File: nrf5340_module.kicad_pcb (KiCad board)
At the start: 4 copper layers, 18.5 x 33 mm, 54 parts, among them J1 U.FL_A-1JB, J2 Conn_01x15, J3 Conn_01x15, J4 Conn_ARM_JTAG_SWD_10, Q1 Q_PMOS_GSD, U1 nrf5340, U2 AP2112K-3.3, Y1 32.768kHz, Y2 32MHz

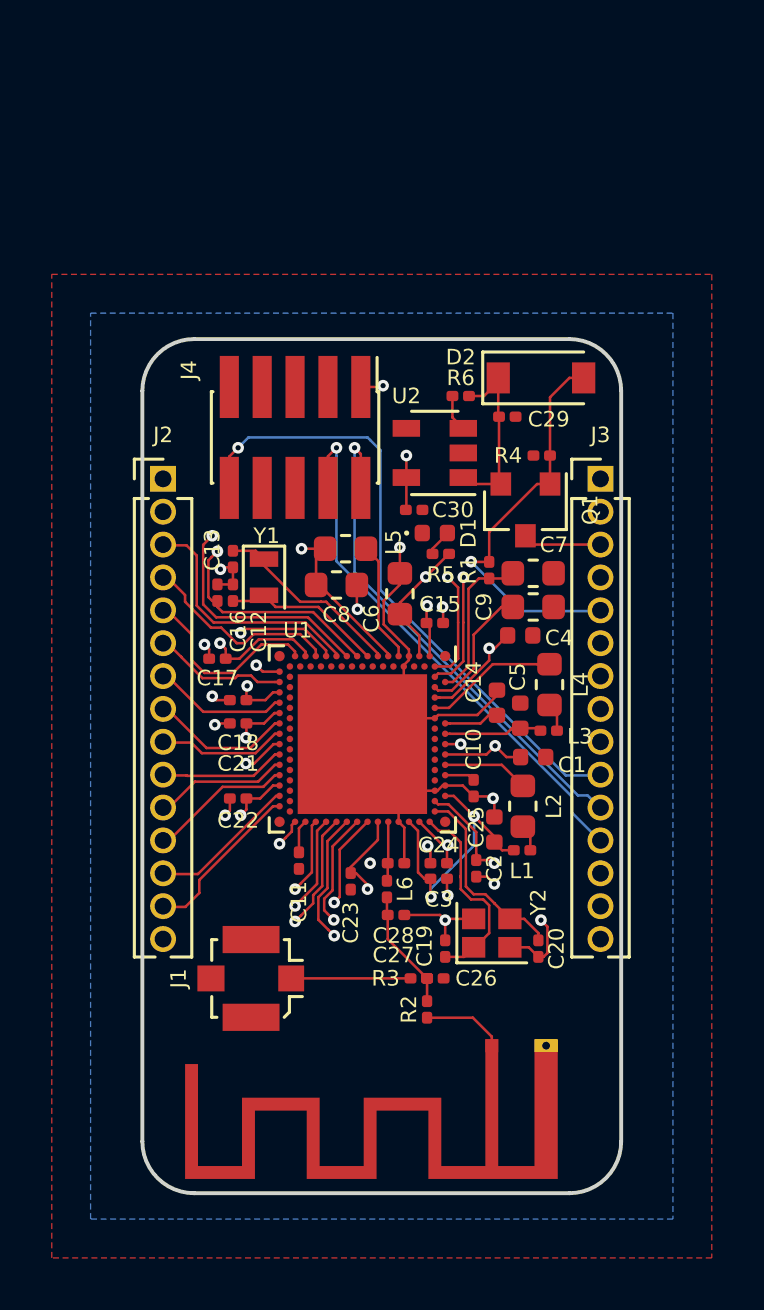
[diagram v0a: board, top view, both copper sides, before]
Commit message: added keepout, stitching, switched layers for better impedance matching
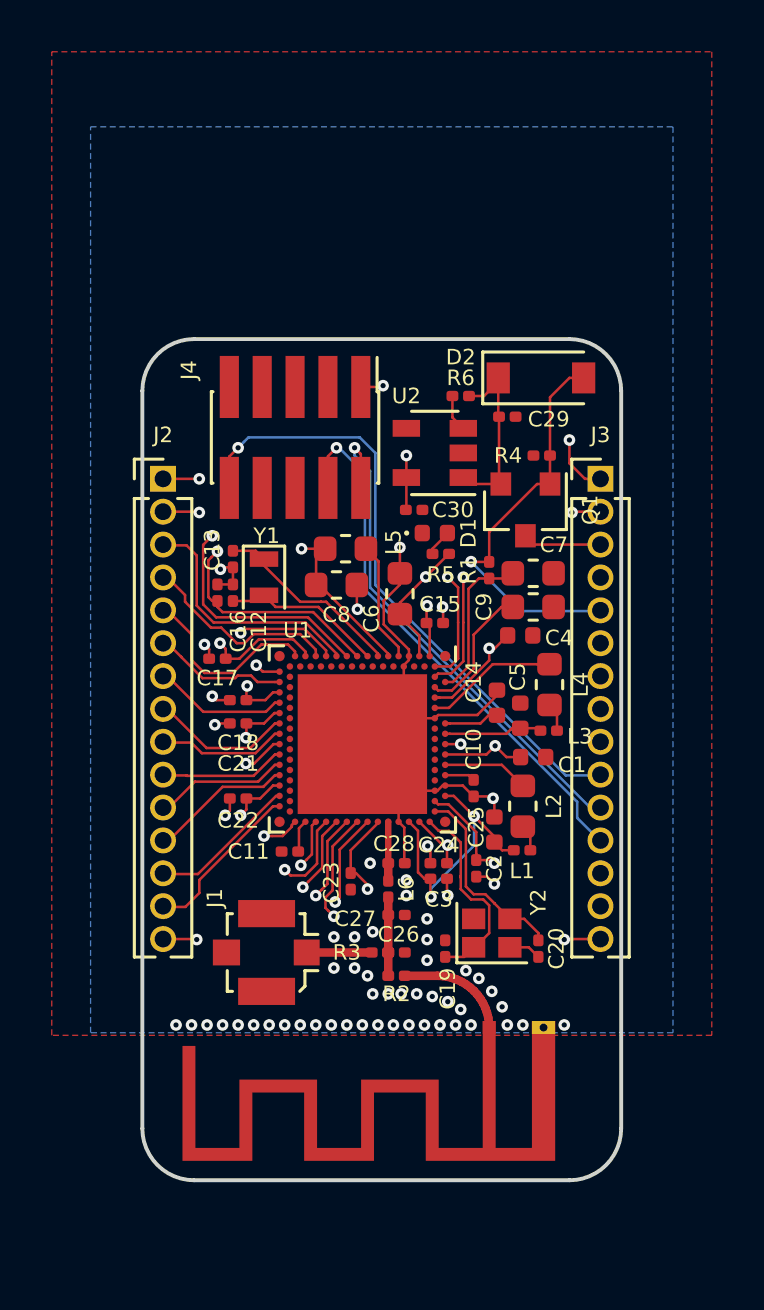
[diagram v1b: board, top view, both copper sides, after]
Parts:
- moved C26 1.80 mm to (229.8, 150.7)
- moved R3 1.80 mm to (229.2, 150.7)
- moved R2 1.76 mm to (229.8, 151.6), turned to 180 degrees
- moved J1 1.17 mm to (224.8, 150.7)
- moved AE1 0.71 mm to (233.4, 153.6)
- moved C11 0.49 mm to (225.7, 146.8), turned to 180 degrees
- moved L6 0.05 mm to (229.5, 148.2)
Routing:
- net SWDCLK: track 40.4 -> 36.9 mm
- net VDD_nRF: track 60.5 -> 63.4 mm, vias 19 -> 21
- net SWDIO: track 39.2 -> 36.3 mm
- net Net-(J1-Pad1): track 4.61 -> 2.51 mm
- net P0.28: track 17.3 -> 15.5 mm
- net Net-(C26-Pad2): track 4.65 -> 3.03 mm
- net Net-(AE1-Pad1): track 3.15 -> 4.40 mm
- net GND: track 41.9 -> 43.0 mm, vias 15 -> 62
- net nRESET: track 42.4 -> 41.4 mm
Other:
- board size 18.5 x 33 mm -> 18.5 x 32.5 mm
- net class RF: clearance 0.3 -> 0.2; trace_width 0.35 -> 0.33

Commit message: update
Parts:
- removed C8: 4.7uF, Capacitor_SMD:C_0603_1608Metric
- added G***: LOGO, custom_footprints:crohloff_logo, B.Cu at (233.1, 130.3)
- added R7: 0R, Resistor_SMD:R_0603_1608Metric, F.Cu at (227.5, 136.5)
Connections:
- U1 pad E1: VDD_nRF -> Net-(R7-Pad1)
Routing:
- net Net-(R7-Pad1): track 0.00 -> 4.41 mm, vias 0 -> 2
- net VDD_nRF: track 63.4 -> 61.5 mm
- net GND: track 43.0 -> 42.1 mm, vias 62 -> 67
